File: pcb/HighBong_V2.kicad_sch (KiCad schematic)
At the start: 18 parts, among them J1 LEDs, J2 Programming header, SW2 Mode Button, U1 AMS1117-3.3, U2 ESP32

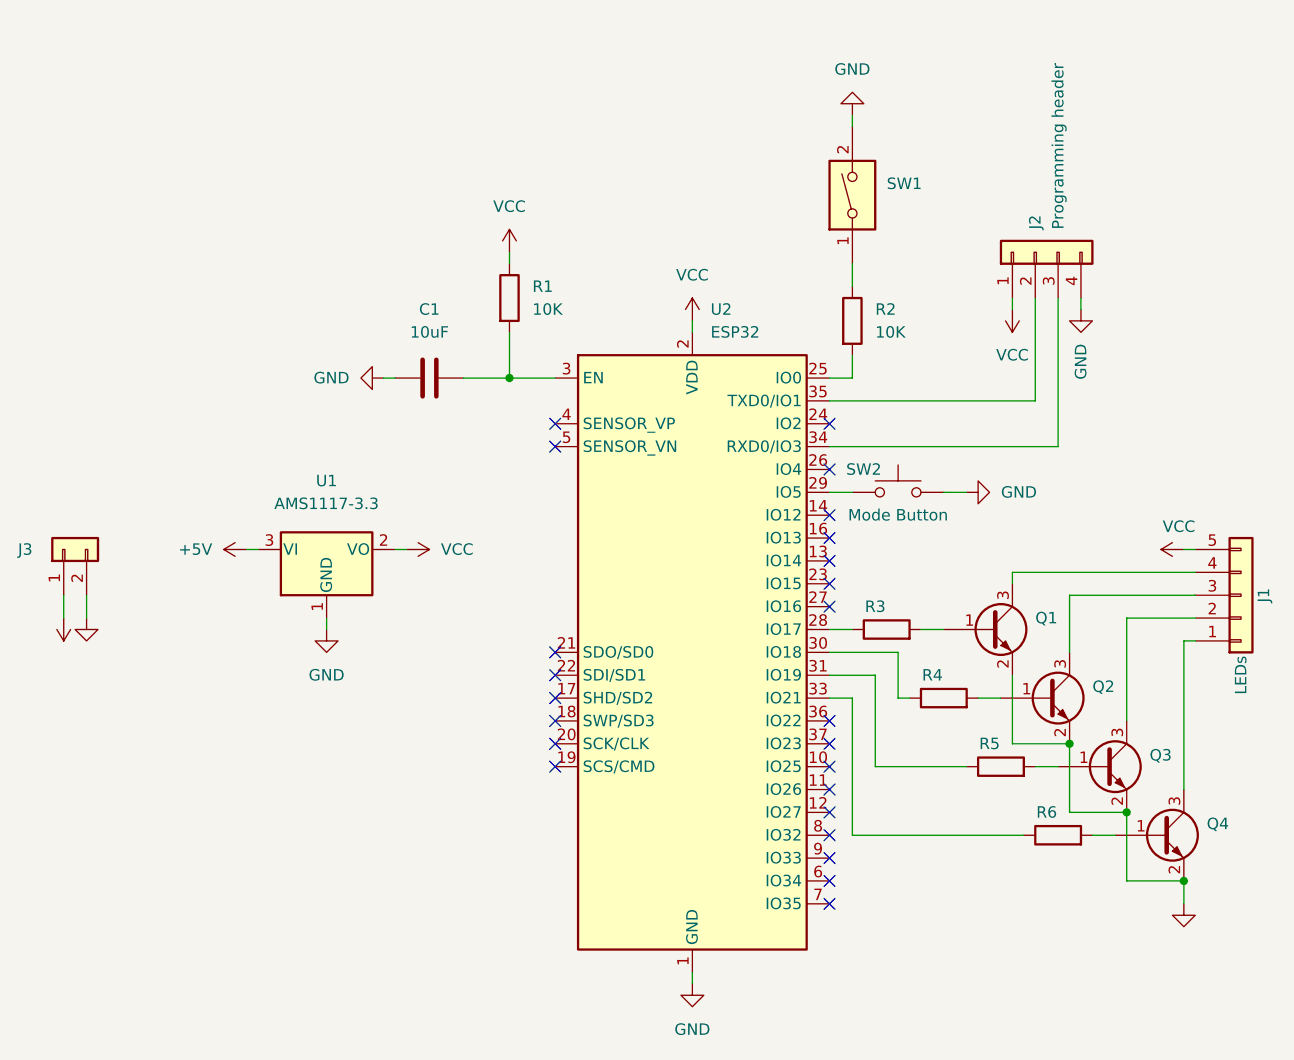
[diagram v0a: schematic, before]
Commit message: Fix issues with drill holes and swtich footprint
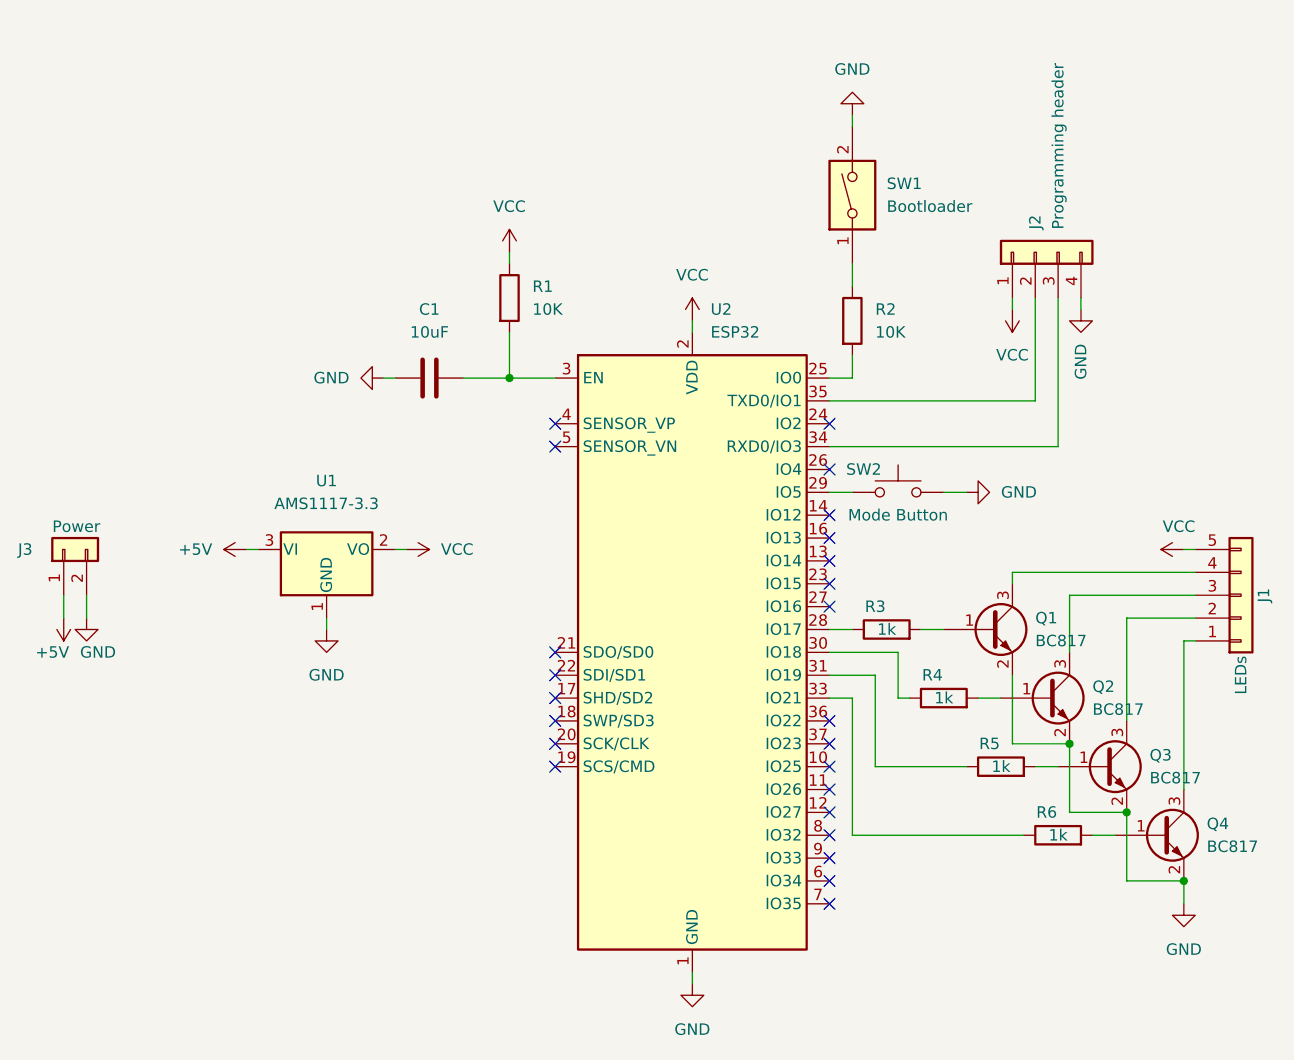
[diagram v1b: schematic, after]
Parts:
- J3: value (none) -> Power; footprint (none) -> Connector_JST:JST_PH_B2B-PH-SM4-TB_1x02-1MP_P2.00mm_Vertical
- Q1, Q2, Q3, Q4: value (none) -> BC817; footprint (none) -> Package_TO_SOT_SMD:SOT-23
- R3, R4, R5, R6: value (none) -> 1k; footprint (none) -> Resistor_SMD:R_0805_2012Metric_Pad1.20x1.40mm_HandSolder
- SW1: value (none) -> Bootloader; footprint footprints:KPS-1290 -> Custom:KPS-1290
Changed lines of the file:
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@@
       (effects (font (size 1.27 1.27)) hide)
     )
-    (property "Value" "" (id 1) (at 156.21 142.24 0))
+    (property "Value" "GND" (id 1) (at 156.21 142.24 0))
     (property "Footprint" "" (id 2) (at 156.21 137.16 0)
       (effects (font (size 1.27 1.27)) hide)
@@
       (effects (font (size 1.27 1.27)) (justify right))
     )
-    (property "Value" "" (id 1) (at 30.48 95.25 90)
+    (property "Value" "Power" (id 1) (at 30.48 95.25 90)
       (effects (font (size 1.27 1.27)) (justify right))
     )
-    (property "Footprint" "" (id 2) (at 31.75 97.79 0)
+    (property "Footprint" "Connector_JST:JST_PH_B2B-PH-SM4-TB_1x02-1MP_P2.00mm_Vertical" (id 2) (at 31.75 97.79 0)
       (effects (font (size 1.27 1.27)) hide)
     )
@@
       (effects (font (size 1.27 1.27)) hide)
     )
-    (property "Value" "" (id 1) (at 35.56 109.22 0))
+    (property "Value" "GND" (id 1) (at 35.56 109.22 0))
     (property "Footprint" "" (id 2) (at 34.29 105.41 0)
       (effects (font (size 1.27 1.27)) hide)
@@
       (effects (font (size 1.27 1.27)) (justify left))
     )
-    (property "Value" "" (id 1) (at 146.05 115.57 0)
-      (effects (font (size 1.27 1.27)) (justify left))
-    )
-    (property "Footprint" "" (id 2) (at 146.05 116.205 0)
+    (property "Value" "BC817" (id 1) (at 146.05 115.57 0)
+      (effects (font (size 1.27 1.27)) (justify left))
+    )
+    (property "Footprint" "Package_TO_SOT_SMD:SOT-23" (id 2) (at 146.05 116.205 0)
       (effects (font (size 1.27 1.27) italic) (justify left) hide)
     )
@@
     (in_bom yes) (on_board yes)
     (property "Reference" "R4" (id 0) (at 128.27 111.76 90))
-    (property "Value" "" (id 1) (at 129.54 114.3 90))
-    (property "Footprint" "" (id 2) (at 129.54 116.078 90)
+    (property "Value" "1k" (id 1) (at 129.54 114.3 90))
+    (property "Footprint" "Resistor_SMD:R_0805_2012Metric_Pad1.20x1.40mm_HandSolder" (id 2) (at 129.54 116.078 90)
       (effects (font (size 1.27 1.27)) hide)
     )
@@
       (effects (font (size 1.27 1.27)) (justify left))
     )
-    (property "Value" "" (id 1) (at 152.4 123.19 0)
-      (effects (font (size 1.27 1.27)) (justify left))
-    )
-    (property "Footprint" "" (id 2) (at 152.4 123.825 0)
+    (property "Value" "BC817" (id 1) (at 152.4 123.19 0)
+      (effects (font (size 1.27 1.27)) (justify left))
+    )
+    (property "Footprint" "Package_TO_SOT_SMD:SOT-23" (id 2) (at 152.4 123.825 0)
       (effects (font (size 1.27 1.27) italic) (justify left) hide)
     )
@@
       (effects (font (size 1.27 1.27)) (justify left))
     )
-    (property "Value" "" (id 1) (at 158.75 130.81 0)
-      (effects (font (size 1.27 1.27)) (justify left))
-    )
-    (property "Footprint" "" (id 2) (at 158.75 131.445 0)
+    (property "Value" "BC817" (id 1) (at 158.75 130.81 0)
+      (effects (font (size 1.27 1.27)) (justify left))
+    )
+    (property "Footprint" "Package_TO_SOT_SMD:SOT-23" (id 2) (at 158.75 131.445 0)
       (effects (font (size 1.27 1.27) italic) (justify left) hide)
     )
@@
       (effects (font (size 1.27 1.27)) (justify right))
     )
-    (property "Value" "" (id 1) (at 123.19 59.6899 90)
+    (property "Value" "Bootloader" (id 1) (at 123.19 59.6899 90)
       (effects (font (size 1.27 1.27)) (justify right))
     )
-    (property "Footprint" "footprints:KPS-1290" (id 2) (at 119.38 58.42 0)
+    (property "Footprint" "Custom:KPS-1290" (id 2) (at 119.38 58.42 0)
       (effects (font (size 1.27 1.27)) hide)
     )
@@
       (effects (font (size 1.27 1.27)) hide)
     )
-    (property "Value" "" (id 1) (at 30.48 109.22 0))
+    (property "Value" "+5V" (id 1) (at 30.48 109.22 0))
     (property "Footprint" "" (id 2) (at 31.75 105.41 0)
       (effects (font (size 1.27 1.27)) hide)
@@
     (in_bom yes) (on_board yes)
     (property "Reference" "R6" (id 0) (at 140.97 127 90))
-    (property "Value" "" (id 1) (at 142.24 129.54 90))
-    (property "Footprint" "" (id 2) (at 142.24 131.318 90)
+    (property "Value" "1k" (id 1) (at 142.24 129.54 90))
+    (property "Footprint" "Resistor_SMD:R_0805_2012Metric_Pad1.20x1.40mm_HandSolder" (id 2) (at 142.24 131.318 90)
       (effects (font (size 1.27 1.27)) hide)
     )
@@
       (effects (font (size 1.27 1.27)) (justify left))
     )
-    (property "Value" "" (id 1) (at 139.7 107.95 0)
-      (effects (font (size 1.27 1.27)) (justify left))
-    )
-    (property "Footprint" "" (id 2) (at 139.7 108.585 0)
+    (property "Value" "BC817" (id 1) (at 139.7 107.95 0)
+      (effects (font (size 1.27 1.27)) (justify left))
+    )
+    (property "Footprint" "Package_TO_SOT_SMD:SOT-23" (id 2) (at 139.7 108.585 0)
       (effects (font (size 1.27 1.27) italic) (justify left) hide)
     )
@@
     (in_bom yes) (on_board yes)
     (property "Reference" "R5" (id 0) (at 134.62 119.38 90))
-    (property "Value" "" (id 1) (at 135.89 121.92 90))
-    (property "Footprint" "" (id 2) (at 135.89 123.698 90)
+    (property "Value" "1k" (id 1) (at 135.89 121.92 90))
+    (property "Footprint" "Resistor_SMD:R_0805_2012Metric_Pad1.20x1.40mm_HandSolder" (id 2) (at 135.89 123.698 90)
       (effects (font (size 1.27 1.27)) hide)
     )
@@
     (in_bom yes) (on_board yes)
     (property "Reference" "R3" (id 0) (at 121.92 104.14 90))
-    (property "Value" "" (id 1) (at 123.19 106.68 90))
-    (property "Footprint" "" (id 2) (at 123.19 108.458 90)
+    (property "Value" "1k" (id 1) (at 123.19 106.68 90))
+    (property "Footprint" "Resistor_SMD:R_0805_2012Metric_Pad1.20x1.40mm_HandSolder" (id 2) (at 123.19 108.458 90)
       (effects (font (size 1.27 1.27)) hide)
     )
@@
     )
     (path "/3d2e1835-e3f3-4fe8-b4ee-90f8281dd2e6"
-      (reference "SW1") (unit 1) (value "Bootloader") (footprint "footprints:KPS-1290")
+      (reference "SW1") (unit 1) (value "Bootloader") (footprint "Custom:KPS-1290")
     )
     (path "/de79fa3b-5a21-4aa0-b062-88deb8e9dcc0"

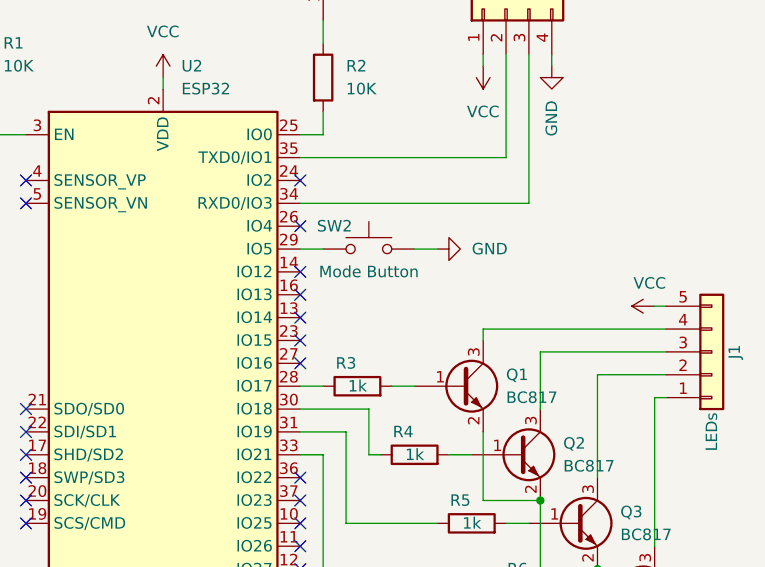
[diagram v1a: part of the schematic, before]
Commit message: Move button to GPIO14
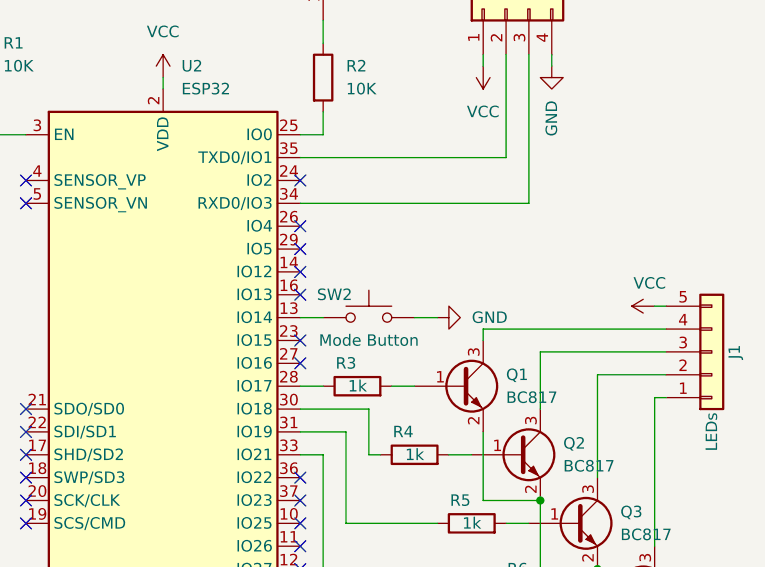
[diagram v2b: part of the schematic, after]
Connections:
- net at U2.13 (IO14): now also SW2.1
- net at U2.29 (IO5): no longer SW2.1
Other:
- moved on the sheet: SW2
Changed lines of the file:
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@@
   (no_connect (at 116.84 88.9))
   (no_connect (at 116.84 101.6))
-  (no_connect (at 116.84 99.06))
   (no_connect (at 116.84 96.52))
   (no_connect (at 116.84 93.98))
@@
   (no_connect (at 116.84 119.38))
   (no_connect (at 116.84 116.84))
+  (no_connect (at 116.84 91.44))
   (no_connect (at 116.84 83.82))
   (no_connect (at 86.36 83.82))
@@
     (stroke (width 0) (type default) (color 0 0 0 0))
   )
+  (wire (pts (xy 116.84 99.06) (xy 119.38 99.06))
+    (stroke (width 0) (type default) (color 0 0 0 0))
+  )
   (wire (pts (xy 137.16 119.38) (xy 143.51 119.38))
     (stroke (width 0) (type default) (color 0 0 0 0))
   )
-  (wire (pts (xy 129.54 91.44) (xy 132.08 91.44))
+  (wire (pts (xy 129.54 99.06) (xy 132.08 99.06))
     (stroke (width 0) (type default) (color 0 0 0 0))
   )
@@
   )
   (wire (pts (xy 133.35 114.3) (xy 135.89 114.3))
-    (stroke (width 0) (type default) (color 0 0 0 0))
-  )
-  (wire (pts (xy 116.84 91.44) (xy 119.38 91.44))
     (stroke (width 0) (type default) (color 0 0 0 0))
   )
@@
     (pin "1")
   )
-  (symbol (lib_id "power:GND") (at 132.08 91.44 90) (unit 1)
-    (in_bom yes) (on_board yes) (fields_autoplaced)
-    (property "Reference" "#PWR0107" (id 0) (at 138.43 91.44 0)
-      (effects (font (size 1.27 1.27)) hide)
-    )
-    (property "Value" "GND" (id 1) (at 135.89 91.4399 90)
+  (symbol (lib_id "power:GND") (at 132.08 99.06 90) (unit 1)
+    (in_bom yes) (on_board yes) (fields_autoplaced)
+    (property "Reference" "#PWR0107" (id 0) (at 138.43 99.06 0)
+      (effects (font (size 1.27 1.27)) hide)
+    )
+    (property "Value" "GND" (id 1) (at 135.89 99.0599 90)
       (effects (font (size 1.27 1.27)) (justify right))
     )
-    (property "Footprint" "" (id 2) (at 132.08 91.44 0)
-      (effects (font (size 1.27 1.27)) hide)
-    )
-    (property "Datasheet" "" (id 3) (at 132.08 91.44 0)
+    (property "Footprint" "" (id 2) (at 132.08 99.06 0)
+      (effects (font (size 1.27 1.27)) hide)
+    )
+    (property "Datasheet" "" (id 3) (at 132.08 99.06 0)
       (effects (font (size 1.27 1.27)) hide)
     )
@@
     (pin "2")
   )
-  (symbol (lib_id "Switch:SW_Push") (at 124.46 91.44 0) (unit 1)
-    (in_bom yes) (on_board yes)
-    (property "Reference" "SW2" (id 0) (at 120.65 88.9 0))
-    (property "Value" "Mode Button" (id 1) (at 124.46 93.98 0))
-    (property "Footprint" "Button_Switch_SMD:SW_Push_1P1T_NO_6x6mm_H9.5mm" (id 2) (at 124.46 86.36 0)
-      (effects (font (size 1.27 1.27)) hide)
-    )
-    (property "Datasheet" "~" (id 3) (at 124.46 86.36 0)
-      (effects (font (size 1.27 1.27)) hide)
-    )
+  (symbol (lib_id "Switch:SW_Push") (at 124.46 99.06 0) (unit 1)
+    (in_bom yes) (on_board yes)
+    (property "Reference" "SW2" (id 0) (at 120.65 96.52 0))
+    (property "Value" "Mode Button" (id 1) (at 124.46 101.6 0))
+    (property "Footprint" "Button_Switch_SMD:SW_Push_1P1T_NO_6x6mm_H9.5mm" (id 2) (at 124.46 93.98 0)
+      (effects (font (size 1.27 1.27)) hide)
+    )
+    (property "Datasheet" "~" (id 3) (at 124.46 93.98 0)
+      (effects (font (size 1.27 1.27)) hide)
+    )
